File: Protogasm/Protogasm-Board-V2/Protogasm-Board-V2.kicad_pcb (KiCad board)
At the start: 2 copper layers, 10 parts, among them J1 Neopixel_Ring_Header, M1 Motor_DC, Q1 FQP30N06L, SW1 Rotary_Encoder_Switch, U1 Arduino_UNO_R3, U2 MPX5050GP

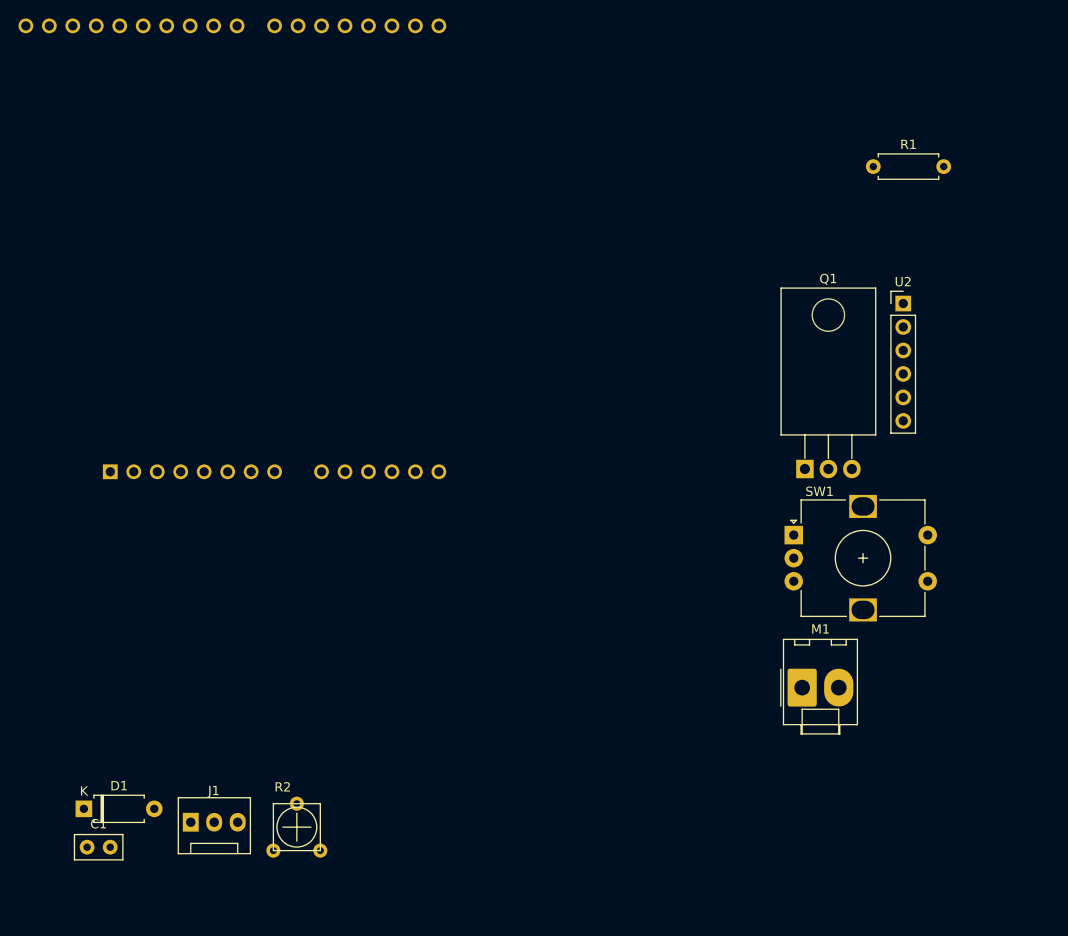
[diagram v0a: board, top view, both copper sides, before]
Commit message: Place components pretty close to where they should be
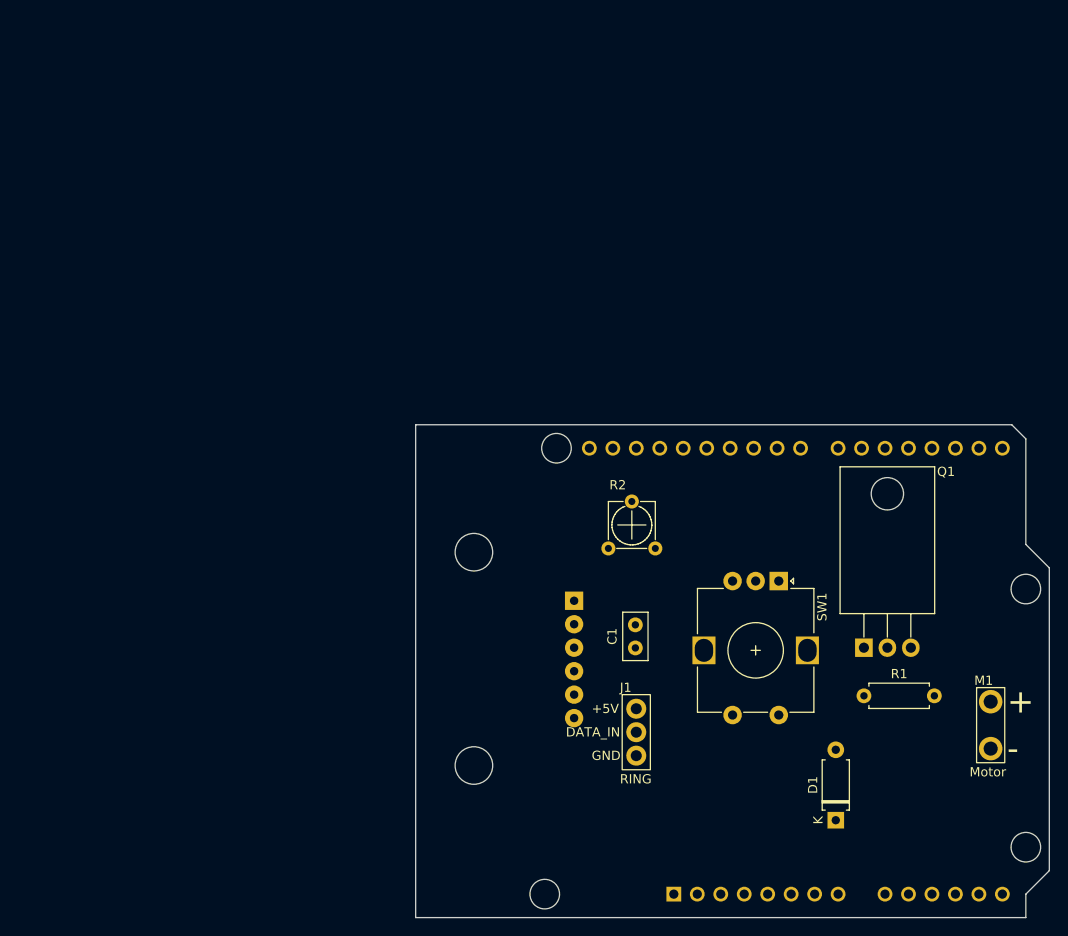
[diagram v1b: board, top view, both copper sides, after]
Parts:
- J1: footprint Connector:FanPinHeader_1x03_P2.54mm_Vertical -> custom-footprints:Neopixel_Ring_WirePins
- M1: footprint Connector_Molex:Molex_KK-396_A-41791-0002_1x02_P3.96mm_Vertical -> custom-footprints:Motor_DC_WirePins
- U1: footprint Module:Arduino_UNO_R3 -> Module:Arduino_UNO_R3_WithMountingHoles
- U2: footprint Connector_PinHeader_2.54mm:PinHeader_1x06_P2.54mm_Vertical -> custom-footprints:MPX5050GP; moved to B.Cu
- moved D1 81.4 mm to (154.7, 113.9), turned to 90 degrees
- moved U1 76.2 mm to (137.2, 121.9)
- moved C1 63.1 mm to (133.0, 95.3), turned to 90 degrees
- moved R1 57.3 mm to (157.7, 100.5)
- moved J1 49.8 mm to (133.1, 101.9)
- moved R2 48.8 mm to (130.1, 84.5)
- moved U2 48.0 mm to (126.4, 90.2), turned to 180 degrees
- moved M1 20.5 mm to (171.5, 101.1)
- moved Q1 20.4 mm to (157.7, 95.2)
- moved SW1 5.23 mm to (148.5, 88.0), turned to -90 degrees
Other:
- board outline added: 68.6 x 53.3 mm

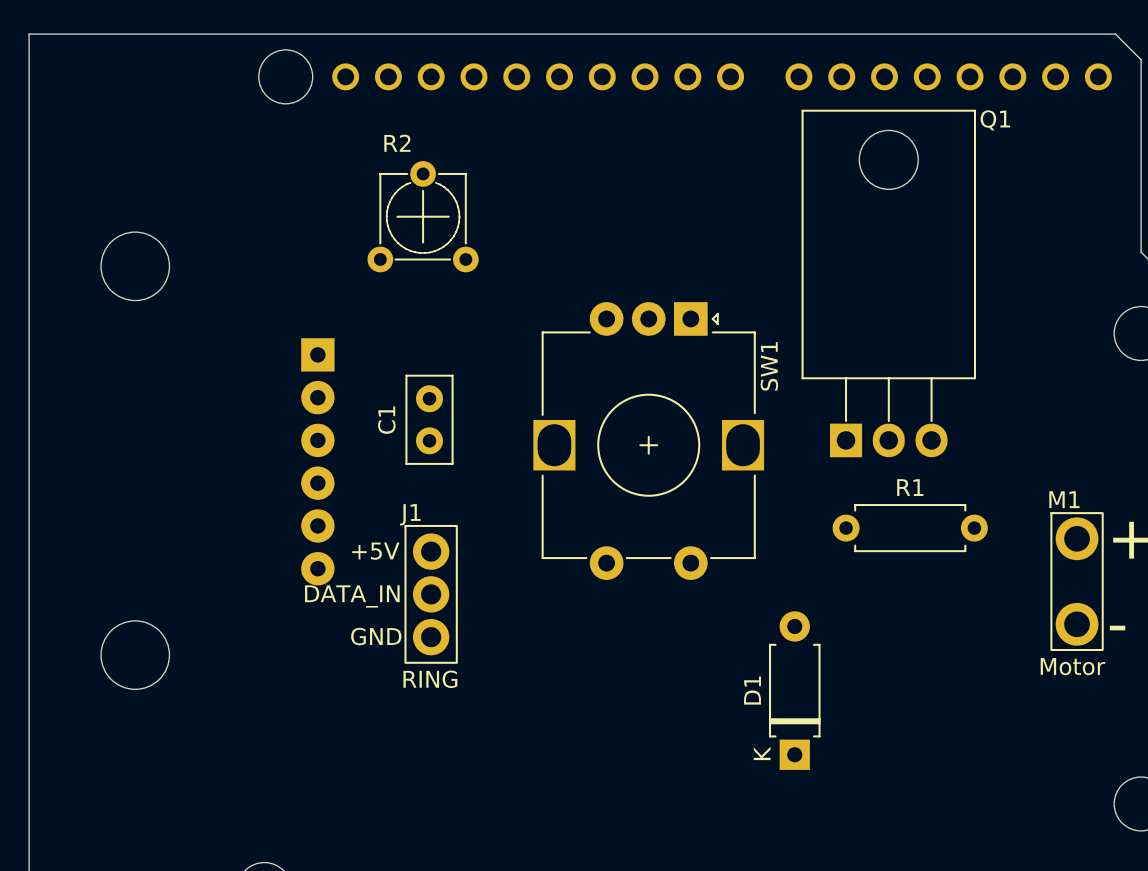
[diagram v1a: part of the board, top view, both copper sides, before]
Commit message: Component placements match V1 exactly
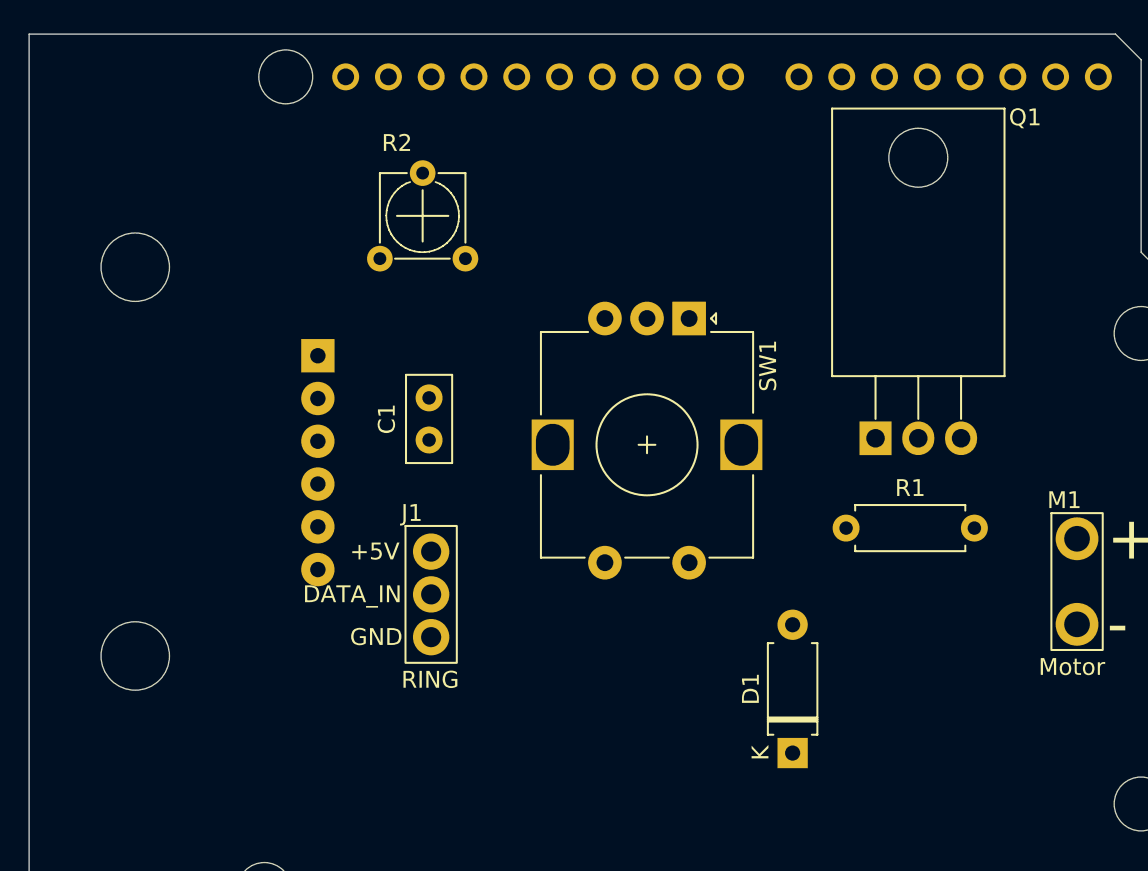
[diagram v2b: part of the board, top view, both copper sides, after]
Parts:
- moved Q1 1.76 mm to (159.5, 95.1)
- moved D1 0.16 mm to (154.6, 113.8)
- moved SW1 0.10 mm to (148.4, 88.0)
- moved R2 0.06 mm to (130.1, 84.5)
- moved C1 0.06 mm to (133.0, 95.2)
- moved U2 0.05 mm to (126.4, 90.2)
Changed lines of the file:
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@@
   )
   (footprint "Rotary_Encoder:RotaryEncoder_Alps_EC12E-Switch_Vertical_H20mm" (layer "F.Cu")
-    (at 148.5178 88.0364 -90)
+    (at 148.4162 88.011 -90)
     (descr "Alps rotary encoder, EC12E... with switch, vertical shaft, http://www.alps.com/prod/info/E/HTML/Encoder/Incremental/EC12E/EC12E1240405.html & http://cdn-reichelt.de/documents/datenblatt/F100/402097STEC12E08.PDF")
     (tags "rotary encoder")
@@
   )
   (footprint "Capacitor_THT:C_Disc_D5.0mm_W2.5mm_P2.50mm" (layer "F.Cu")
-    (at 132.9984 95.2754 90)
+    (at 132.973 95.2246 90)
     (descr "C, Disc series, Radial, pin pitch=2.50mm, , diameter*width=5*2.5mm^2, Capacitor, http://cdn-reichelt.de/documents/datenblatt/B300/DS_KERKO_TC.pdf")
     (tags "C Disc series Radial pin pitch 2.50mm  diameter 5mm width 2.5mm Capacitor")
@@
   )
   (footprint "Package_TO_SOT_THT:TO-220-3_Horizontal_TabDown" (layer "F.Cu")
-    (at 157.734 95.25)
+    (at 159.4866 95.123)
     (descr "TO-220-3, Horizontal, RM 2.54mm, see https://www.vishay.com/docs/66542/to-220-1.pdf")
     (tags "TO-220-3 Horizontal RM 2.54mm")
@@
   )
   (footprint "Diode_THT:D_A-405_P7.62mm_Horizontal" (layer "F.Cu")
-    (at 154.69 113.919 90)
+    (at 154.563 113.8174 90)
     (descr "Diode, A-405 series, Axial, Horizontal, pin pitch=7.62mm, , length*diameter=5.2*2.7mm^2, , http://www.diodes.com/_files/packages/A-405.pdf")
     (tags "Diode A-405 series Axial Horizontal pin pitch 7.62mm  length 5.2mm diameter 2.7mm")
@@
   )
   (footprint "custom-footprints:uxcell_TRIMPOT" (layer "F.Cu")
-    (at 130.0774 84.5058)
+    (at 130.052 84.455)
     (property "Sheetfile" "Protogasm-Board-V2.kicad_sch")
     (property "Sheetname" "")
@@
   )
   (footprint "custom-footprints:MPX5050GP" (layer "B.Cu")
-    (at 126.369 90.17 180)
-    (property "Sheetfile" "Protogasm-Board-V2.kicad_sch")
-    (property "Sheetname" "")
+    (at 126.369 90.2208 180)
+    (property "Sheetfile" "Protogasm-Board-V2.kicad_sch")
+    (property "Sheetname" "")

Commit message: Reroute board
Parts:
- moved R1 7.62 mm to (165.4, 100.5), turned to 180 degrees
- moved J1 2.03 mm to (133.1, 103.9)
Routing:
- net GND: track 0.00 -> 100.6 mm
- net Net-(U1-Pad9): track 0.00 -> 62.0 mm, vias 0 -> 1
- net +5V: track 0.00 -> 54.8 mm
- net Net-(J1-Pad2): track 0.00 -> 46.1 mm
- net Net-(SW1-PadS2): track 0.00 -> 45.4 mm, vias 0 -> 1
- net Net-(Q1-Pad1): track 0.00 -> 39.8 mm
- net Net-(D1-Pad2): track 0.00 -> 31.1 mm
- net +12V: track 0.00 -> 30.4 mm
- net Net-(SW1-PadB): track 0.00 -> 27.6 mm
- net Net-(SW1-PadA): track 0.00 -> 26.5 mm
- net Net-(R2-Pad2): track 0.00 -> 5.93 mm
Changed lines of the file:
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@@
   )
   (setup
+    (stackup
+      (layer "F.SilkS" (type "Top Silk Screen"))
+      (layer "F.Paste" (type "Top Solder Paste"))
+      (layer "F.Mask" (type "Top Solder Mask") (thickness 0.01))
+      (layer "F.Cu" (type "copper") (thickness 0.035))
+      (layer "dielectric 1" (type "core") (thickness 1.51) (material "FR4") (epsilon_r 4.5) (loss_tangent 0.02))
+      (layer "B.Cu" (type "copper") (thickness 0.035))
+      (layer "B.Mask" (type "Bottom Solder Mask") (thickness 0.01))
+      (layer "B.Paste" (type "Bottom Solder Paste"))
+      (layer "B.SilkS" (type "Bottom Silk Screen"))
+      (copper_finish "None")
+      (dielectric_constraints no)
+    )
     (pad_to_mask_clearance 0)
+    (grid_origin 137.16 121.92)
     (pcbplotparams
       (layerselection 0x00010fc_ffffffff)
@@
   (net 36 "unconnected-(U2-Pad6)")
   (footprint "Resistor_THT:R_Axial_DIN0207_L6.3mm_D2.5mm_P7.62mm_Horizontal" (layer "F.Cu")
-    (at 157.738 100.457)
+    (at 165.358 100.457 180)
     (descr "Resistor, Axial_DIN0207 series, Axial, Horizontal, pin pitch=7.62mm, 0.25W = 1/4W, length*diameter=6.3*2.5mm^2, http://cdn-reichelt.de/documents/datenblatt/B400/1_4W%23YAG.pdf")
     (tags "Resistor Axial_DIN0207 series Axial Horizontal pin pitch 7.62mm 0.25W = 1/4W length 6.3mm diameter 2.5mm")
@@
     (fp_line (start 7.62 0) (end 6.96 0) (layer "F.Fab") (width 0.1))
     (fp_line (start 0 0) (end 0.66 0) (layer "F.Fab") (width 0.1))
-    (pad "1" thru_hole circle (at 0 0) (size 1.6 1.6) (drill 0.8) (layers *.Cu *.Mask)
+    (pad "1" thru_hole circle (at 0 0 180) (size 1.6 1.6) (drill 0.8) (layers *.Cu *.Mask)
       (net 6 "Net-(Q1-Pad1)") (pintype "passive"))
-    (pad "2" thru_hole oval (at 7.62 0) (size 1.6 1.6) (drill 0.8) (layers *.Cu *.Mask)
+    (pad "2" thru_hole oval (at 7.62 0 180) (size 1.6 1.6) (drill 0.8) (layers *.Cu *.Mask)
       (net 2 "GND") (pintype "passive"))
     (model "${KICAD6_3DMODEL_DIR}/Resistor_THT.3dshapes/R_Axial_DIN0207_L6.3mm_D2.5mm_P7.62mm_Horizontal.wrl"
@@
   )
   (footprint "custom-footprints:Neopixel_Ring_WirePins" (layer "F.Cu")
-    (at 133.096 101.854)
+    (at 133.096 103.886)
     (property "Sheetfile" "Protogasm-Board-V2.kicad_sch")
     (property "Sheetname" "")
@@
   (gr_line (start 177.8 86.614) (end 175.26 84.074) (layer "Edge.Cuts") (width 0.05))
   (gr_line (start 175.26 124.46) (end 175.26 121.92) (layer "Edge.Cuts") (width 0.05))
+  (segment (start 132.973 95.2246) (end 132.973 103.763) (width 0.381) (layer "F.Cu") (net 1))
+  (segment (start 132.973 103.763) (end 133.096 103.886) (width 0.381) (layer "F.Cu") (net 1))
+  (segment (start 126.4452 95.2246) (end 126.369 95.3008) (width 0.381) (layer "F.Cu") (net 1))
+  (segment (start 132.973 95.2246) (end 126.4452 95.2246) (width 0.381) (layer "F.Cu") (net 1))
+  (segment (start 131.318 105.664) (end 131.318 109.474) (width 0.381) (layer "B.Cu") (net 1))
+  (segment (start 131.318 109.474) (end 142.24 120.396) (width 0.381) (layer "B.Cu") (net 1))
+  (segment (start 133.096 103.886) (end 131.318 105.664) (width 0.381) (layer "B.Cu") (net 1))
+  (segment (start 132.973 95.2246) (end 130.052 92.3036) (width 0.381) (layer "B.Cu") (net 1))
+  (segment (start 145.796 120.396) (end 147.32 121.92) (width 0.381) (layer "B.Cu") (net 1))
+  (segment (start 142.24 120.396) (end 145.796 120.396) (width 0.381) (layer "B.Cu") (net 1))
+  (segment (start 130.052 92.3036) (end 130.052 84.455) (width 0.381) (layer "B.Cu") (net 1))
+  (segment (start 132.973 92.7246) (end 126.4052 92.7246) (width 0.381) (layer "F.Cu") (net 2))
+  (segment (start 141.4634 92.7246) (end 132.973 92.7246) (width 0.381) (layer "F.Cu") (net 2))
+  (segment (start 145.9162 88.011) (end 145.9162 88.2718) (width 0.381) (layer "F.Cu") (net 2))
+  (segment (start 157.738 100.457) (end 150.4702 100.457) (width 0.381) (layer "F.Cu") (net 2))
+  (segment (start 145.9162 88.011) (end 145.9162 88.2582) (width 0.381) (layer "F.Cu") (net 2))
+  (segment (start 134.874 94.6256) (end 134.874 107.188) (width 0.381) (layer "F.Cu") (net 2))
+  (segment (start 145.9162 88.2582) (end 149.098 91.44) (width 0.381) (layer "F.Cu") (net 2))
+  (segment (start 164.5666 95.123) (end 159.2326 100.457) (width 0.381) (layer "F.Cu") (net 2))
+  (segment (start 132.973 92.7246) (end 134.874 94.6256) (width 0.381) (layer "F.Cu") (net 2))
+  (segment (start 126.4052 92.7246) (end 126.369 92.7608) (width 0.381) (layer "F.Cu") (net 2))
+  (segment (start 160.8836 91.44) (end 164.5666 95.123) (width 0.381) (layer "F.Cu") (net 2))
+  (segment (start 159.2326 100.457) (end 157.738 100.457) (width 0.381) (layer "F.Cu") (net 2))
+  (segment (start 145.9162 88.2718) (end 141.4634 92.7246) (width 0.381) (layer "F.Cu") (net 2))
+  (segment (start 134.874 107.188) (end 133.096 108.966) (width 0.381) (layer "F.Cu") (net 2))
+  (segment (start 150.4702 100.457) (end 148.4162 102.511) (width 0.381) (layer "F.Cu") (net 2))
+  (segment (start 149.098 91.44) (end 160.8836 91.44) (width 0.381) (layer "F.Cu") (net 2))
+  (segment (start 135.64 83.947) (end 135.132 84.455) (width 0.381) (layer "B.Cu") (net 2))
+  (segment (start 135.132 90.5656) (end 132.973 92.7246) (width 0.381) (layer "B.Cu") (net 2))
+  (segment (start 135.64 73.66) (end 135.64 83.947) (width 0.381) (layer "B.Cu") (net 2))
+  (segment (start 135.132 84.455) (end 135.132 90.5656) (width 0.381) (layer "B.Cu") (net 2))
+  (segment (start 154.94 121.92) (end 154.94 114.1944) (width 0.381) (layer "B.Cu") (net 3))
+  (segment (start 154.94 114.1944) (end 154.563 113.8174) (width 0.381) (layer "B.Cu") (net 3))
+  (segment (start 158.7286 113.8174) (end 171.454 101.092) (width 0.381) (layer "B.Cu") (net 3))
+  (segment (start 154.563 113.8174) (end 158.7286 113.8174) (width 0.381) (layer "B.Cu") (net 3))
+  (segment (start 154.563 106.1974) (end 171.4286 106.1974) (width 0.25) (layer "F.Cu") (net 4))
+  (segment (start 171.4286 106.1974) (end 171.454 106.172) (width 0.25) (layer "F.Cu") (net 4))
+  (segment (start 154.563 106.1974) (end 162.0266 98.7338) (width 0.25) (layer "B.Cu") (net 4))
+  (segment (start 162.0266 98.7338) (end 162.0266 95.123) (width 0.25) (layer "B.Cu") (net 4))
+  (segment (start 141.374343 106.426) (end 149.740711 98.059632) (width 0.25) (layer "B.Cu") (net 5))
+  (segment (start 149.740711 77.600711) (end 145.8 73.66) (width 0.25) (layer "B.Cu") (net 5))
+  (segment (start 149.740711 98.059632) (end 149.740711 77.600711) (width 0.25) (layer "B.Cu") (net 5))
+  (segment (start 133.096 106.426) (end 141.374343 106.426) (width 0.25) (layer "B.Cu") (net 5))
+  (segment (start 165.358 100.457) (end 166.157999 99.657001) (width 0.25) (layer "B.Cu") (net 6))
+  (segment (start 159.4866 84.8066) (end 148.34 73.66) (width 0.25) (layer "B.Cu") (net 6))
+  (segment (start 166.157999 94.783999) (end 165.11848 93.74448) (width 0.25) (layer "B.Cu") (net 6))
+  (segment (start 165.11848 93.74448) (end 160.86512 93.74448) (width 0.25) (layer "B.Cu") (net 6))
+  (segment (start 159.4866 95.123) (end 159.4866 84.8066) (width 0.25) (layer "B.Cu") (net 6))
+  (segment (start 160.86512 93.74448) (end 159.4866 95.123) (width 0.25) (layer "B.Cu") (net 6))
+  (segment (start 166.157999 99.657001) (end 166.157999 94.783999) (width 0.25) (layer "B.Cu") (net 6))
+  (segment (start 133.1 78.867) (end 132.592 79.375) (width 0.25) (layer "B.Cu") (net 7))
+  (segment (start 133.1 73.66) (end 133.1 78.867) (width 0.25) (layer "B.Cu") (net 7))
+  (segment (start 142.24 76.924511) (end 143.980511 75.184) (width 0.25) (layer "F.Cu") (net 8))
+  (segment (start 143.980511 75.184) (end 158.496 75.184) (width 0.25) (layer "F.Cu") (net 8))
+  (segment (start 158.496 75.184) (end 160.02 73.66) (width 0.25) (layer "F.Cu") (net 8))
+  (via (at 142.24 76.924511) (size 0.8) (drill 0.4) (layers "F.Cu" "B.Cu") (net 8))
+  (segment (start 142.24 76.924511) (end 142.091689 76.924511) (width 0.25) (layer "B.Cu") (net 8))
+  (segment (start 143.4162 102.511) (end 142.091689 101.186489) (width 0.25) (layer "B.Cu") (net 8))
+  (segment (start 142.091689 101.186489) (end 142.091689 76.924511) (width 0.25) (layer "B.Cu") (net 8))
+  (segment (start 162.421521 76.338479) (end 165.1 73.66) (width 0.25) (layer "F.Cu") (net 9))
+  (segment (start 155.088721 76.338479) (end 162.421521 76.338479) (width 0.25) (layer "F.Cu") (net 9))
+  (segment (start 143.4162 88.011) (end 155.088721 76.338479) (width 0.25) (layer "F.Cu") (net 9))
+  (segment (start 155.483127 88.011) (end 148.4162 88.011) (width 0.25) (layer "F.Cu") (net 10))
+  (segment (start 167.64 75.854127) (end 155.483127 88.011) (width 0.25) (layer "F.Cu") (net 10))
+  (segment (start 167.64 73.66) (end 167.64 75.854127) (width 0.25) (layer "F.Cu") (net 10))
+  (segment (start 157.48 119.38) (end 160.02 121.92) (width 0.25) (layer "F.Cu") (net 23))
+  (segment (start 129.54 119.38) (end 157.48 119.38) (width 0.25) (layer "F.Cu") (net 23))
+  (via (at 129.54 119.38) (size 0.8) (drill 0.4) (layers "F.Cu" "B.Cu") (free) (net 23))
+  (segment (start 128.778 92.6298) (end 128.778 118.618) (width 0.25) (layer "B.Cu") (net 23))
+  (segment (start 126.369 90.2208) (end 128.778 92.6298) (width 0.25) (layer "B.Cu") (net 23))
+  (segment (start 128.778 118.618) (end 129.54 119.38) (width 0.25) (layer "B.Cu") (net 23))
 )
